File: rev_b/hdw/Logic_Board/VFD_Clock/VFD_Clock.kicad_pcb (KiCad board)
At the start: 4 copper layers, 200 x 50 mm, 359 parts, among them J1501 PICKIT4, J1801 I2C, J1802 USB UART, J201 +12V IN, J2401 USB_B_Mini, J3001 DSP_IO_Connector, Q1001 IRFL214TRPBF, Q1301 BSS214NW, Q1302 ZXMS6004FFTA, Q1304 BSS214NW, Q1306 ZXMS6004FFTA, Q1307 BSS214NW, Q1308 ZXMS6004FFTA, Q1501 BSS214NW, Q1801 BSS214NW, SW1501 MRST, U1001 TLV6700, U1002 LT3757, U1101 MCP9804, U1103 LTC4151DD, U1401 PIC32MZ2048EFG100_IPT, U1801 LTC6900, U1802 74LVC1G97, U1803 MCP9804, U1901 DS3231MZ, U1902 TLV6700, U2001 74LVC1G97, U2003 74LVC1G97, U2004 74LVC1G97, U2006 74LVC1G97, U201 TPS26600RHFT, U2101 TPS71533, U2102 74LVC1G97, U2103 74LVC1G97, U2104 74LVC1G97, U2105 74LVC1G97, U2106 74LVC1G97, U2107 74LVC1G97, U2108 74LVC1G97, U2201 TCA9803, U2301 DS1683, U2401 TLV6700, U2402 FT234XD, U2403 TPD3S014DBVR, U2404 SN74AVC2T245, U2601 INA219BxDCN, U2602 MCP9804, U2801 74VHC541, U2802 74VHC541, U2803 74LVC1G97, U2804 74LVC1G97, U2901 TCA9803, U2902 74VHC541, U301 INA219BxDCN, U302 MCP9804, U401 TPS62150A, U502 MCP9804, U503 INA219BxDCN, U601 TPS62150A, U702 MCP9804, U703 INA219BxDCN, U801 TPS62150A, U902 MCP9804, U903 INA219BxDCN, X1701 ASE-8.000MHz, X1702 ECS-327KE

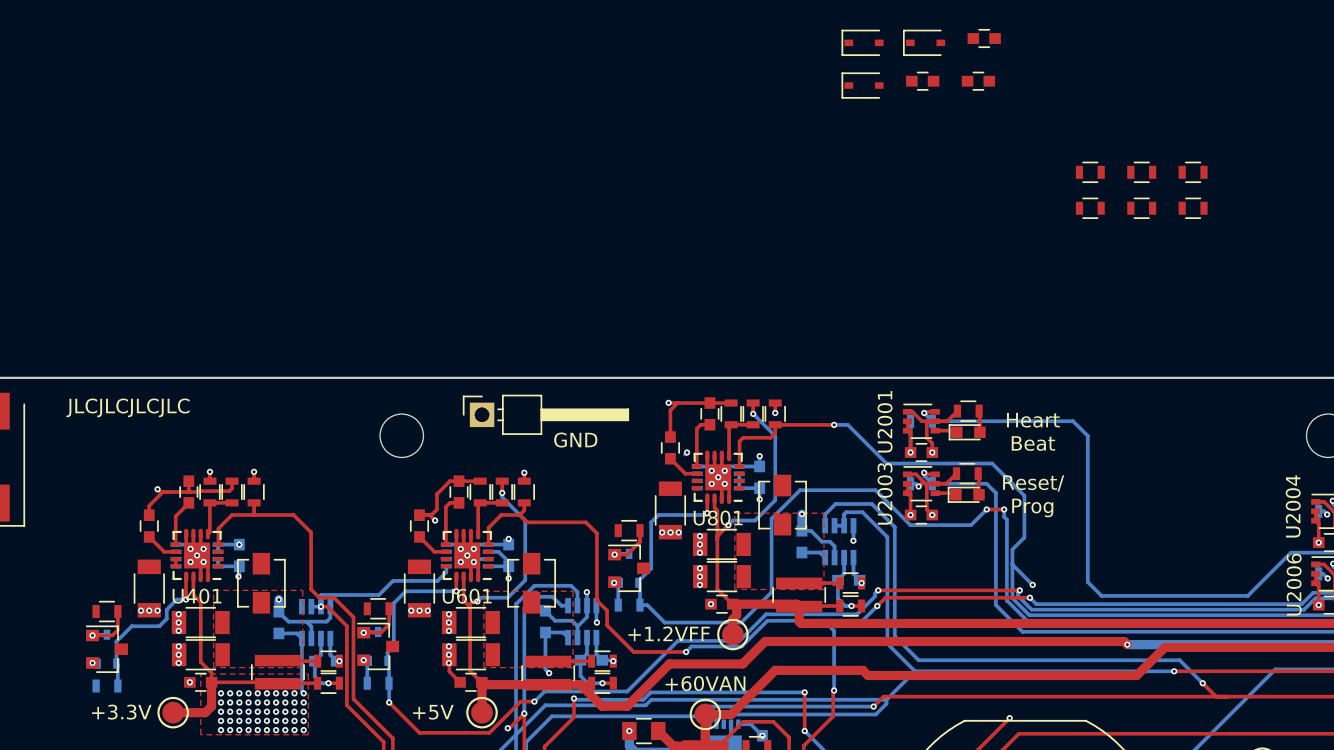
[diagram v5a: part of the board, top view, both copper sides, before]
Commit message: finished placing new parts
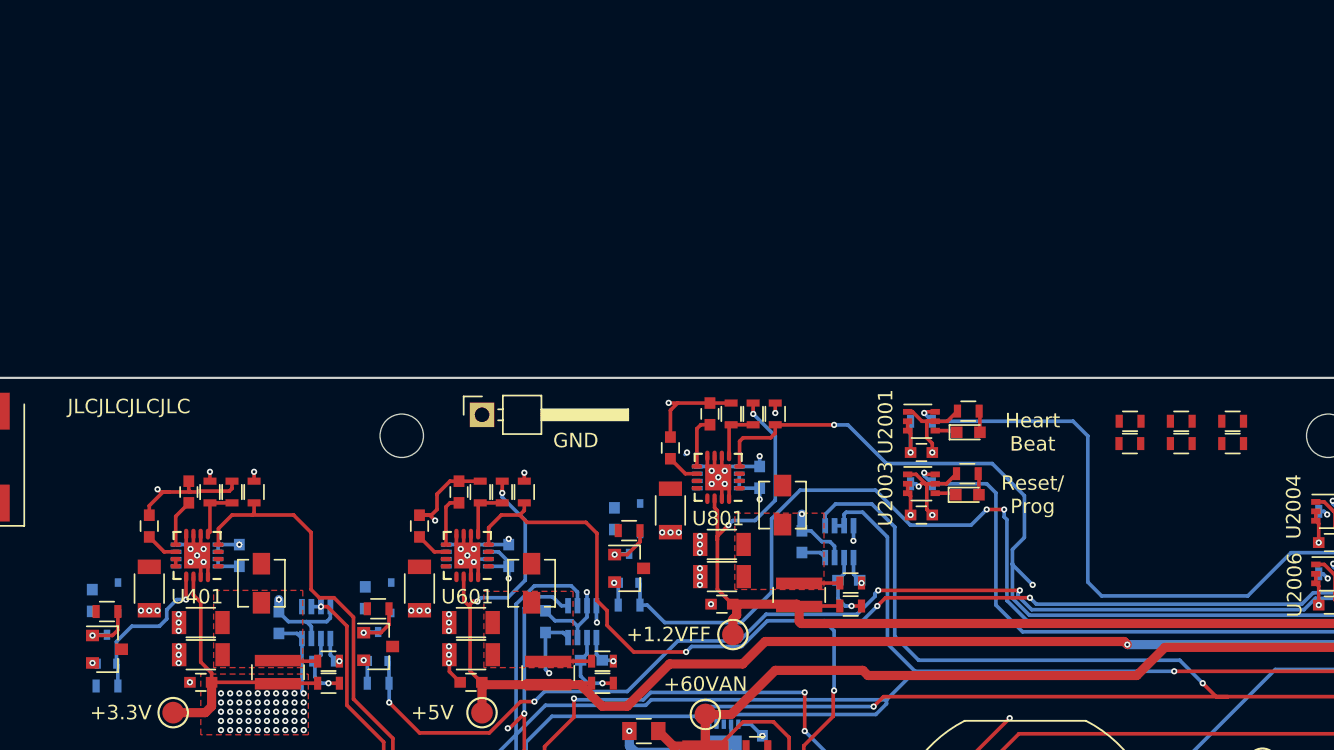
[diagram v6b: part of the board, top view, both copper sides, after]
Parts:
- C1301, C1302, C1303, D1301, D1302, D1303: moved to B.Cu
- moved C1301 67.7 mm to (81.0, 81.7), turned to 90 degrees
- moved D1301 64.2 mm to (82.7, 81.5), turned to 90 degrees
- moved C1302 57.6 mm to (99.8, 81.5), turned to 90 degrees
- moved D1302 48.2 mm to (101.6, 81.5), turned to 90 degrees
- moved C1303 39.3 mm to (117.0, 76.0), turned to 90 degrees
- moved D1303 38.3 mm to (118.8, 76.0), turned to 90 degrees
- moved R1802 17.4 mm to (152.7, 69.3)
- moved R1808 17.4 mm to (156.2, 69.3)
- moved R1810 17.4 mm to (159.7, 69.3)
- moved R1803 16.5 mm to (152.6, 70.8)
- moved R1809 16.5 mm to (156.2, 70.8)
- moved R1811 16.5 mm to (159.7, 70.8)
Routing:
- net I2C_SDA: track 257.9 -> 247.4 mm
- net POS5_RUN: track 119.2 -> 109.4 mm, vias 6 -> 5
- net POS1P2_VFF_RUN: track 105.6 -> 95.9 mm, vias 4 -> 3
- net +3V3: track 175.6 -> 174.8 mm, vias 88 -> 87

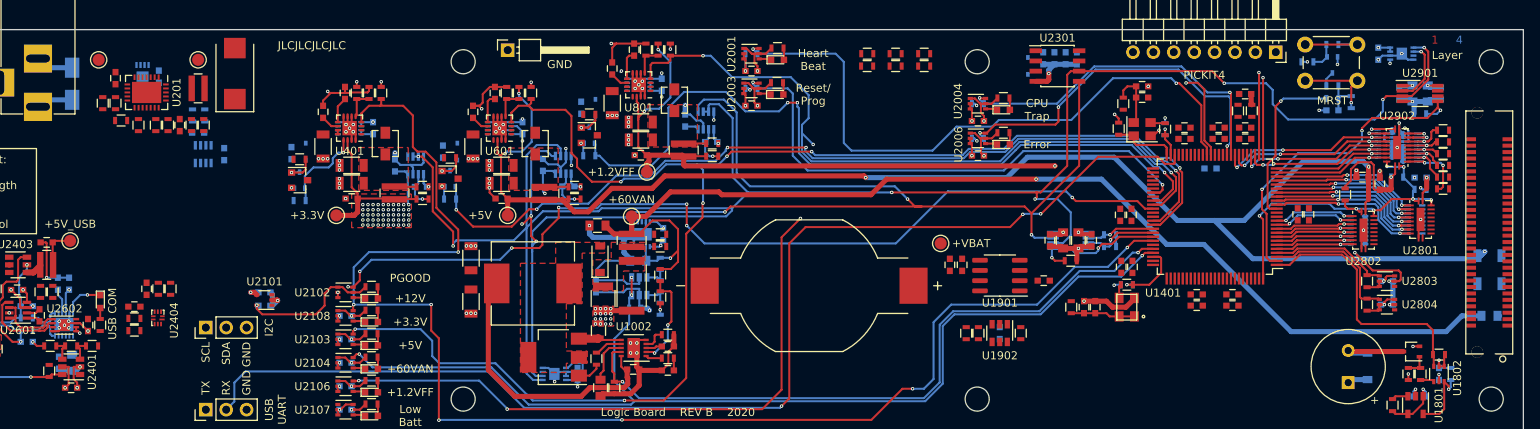
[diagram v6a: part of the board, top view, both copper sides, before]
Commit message: More rev B PCB routing
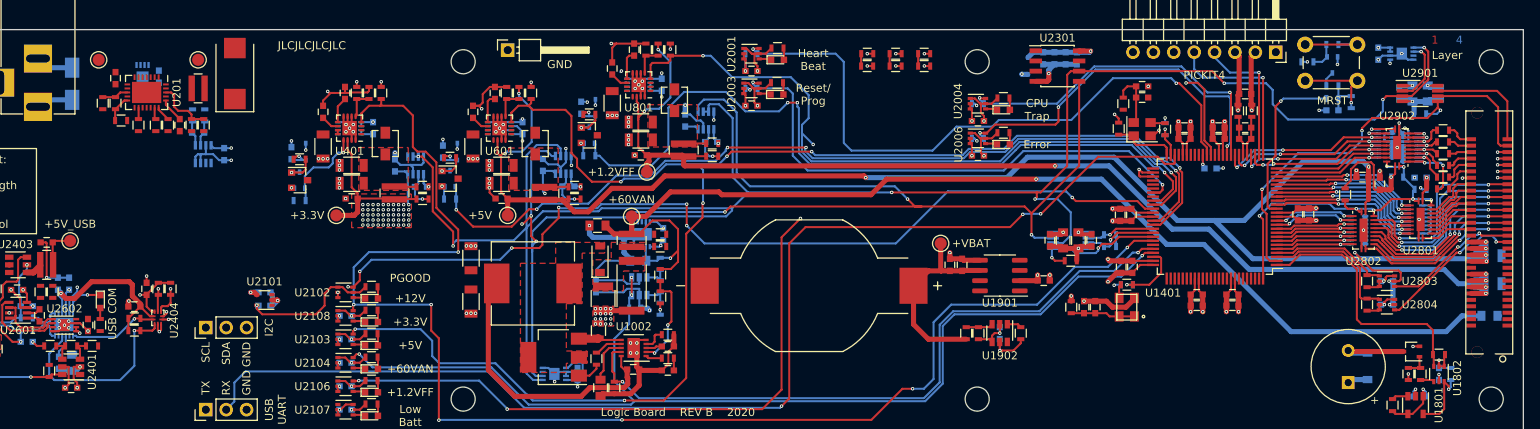
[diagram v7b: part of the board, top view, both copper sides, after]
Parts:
- turned R205 to 90 degrees
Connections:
- U1401 pad 70: Net-(U1401-Pad70) -> POS5_USB_PGOOD
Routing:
- net GND: track 280.5 -> 378.0 mm, vias 147 -> 178
- net +1.2VFF: track 77.5 -> 151.6 mm, vias 3 -> 7
- net +3V3: track 174.8 -> 240.1 mm, vias 87 -> 108
- net USB_UART_TX_BUF: track 0.00 -> 24.7 mm, vias 0 -> 1
- net VBAT: track 0.00 -> 24.6 mm
- net Grid_0_DSP: track 0.00 -> 24.3 mm, vias 0 -> 2
- net Grid_1_DSP: track 0.00 -> 23.6 mm, vias 0 -> 2
- net Grid_2_DSP: track 0.00 -> 22.8 mm, vias 0 -> 2
- net +3.3V_USB: track 3.15 -> 25.8 mm, vias 0 -> 1
- net Grid_3_DSP: track 0.00 -> 22.0 mm, vias 0 -> 2
- net Grid_4_DSP: track 0.00 -> 21.2 mm, vias 0 -> 2
- net Colon_1_DSP: track 0.00 -> 20.5 mm, vias 0 -> 2
- net Grid_5_DSP: track 0.00 -> 20.4 mm, vias 0 -> 2
- net Colon_0_DSP: track 0.00 -> 19.7 mm, vias 0 -> 2
- net Colon_3_DSP: track 0.00 -> 18.3 mm, vias 0 -> 2
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
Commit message: moar rev b rowting
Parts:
- turned R2406 to 90 degrees
- turned R2410 to 90 degrees
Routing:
- net GND: track 378.0 -> 409.4 mm, vias 178 -> 201
- net +5V_USB: track 8.24 -> 34.5 mm, vias 1 -> 4
- net VBAT_PGOOD: track 1.82 -> 27.2 mm
- net +12V: track 43.8 -> 57.5 mm, vias 1 -> 2
- net +60VAN: track 144.6 -> 158.0 mm, vias 2 -> 6
- net Net-(L2401-Pad2): track 0.00 -> 6.29 mm
- net +3V3: track 240.1 -> 246.3 mm, vias 108 -> 110
- net POS5_USB_SNS-: track 1.75 -> 6.47 mm
- net POS5_USB_SNS+: track 1.76 -> 5.41 mm
- net Net-(R205-Pad2): track 0.00 -> 2.66 mm, vias 0 -> 1
- net Net-(R2407-Pad2): track 2.16 -> 4.74 mm
- net POS12_PGOOD: track 121.3 -> 120.7 mm
- added copper zone on F.Cu, net +12V
- added copper zone on F.Cu, net +12Vin
- added copper zone on F.Cu, net Net-(L401-Pad1)
- added copper zone on F.Cu, net Net-(L601-Pad1)
- added copper zone on F.Cu, net Net-(L801-Pad1)
- added copper zone on F.Cu, net Net-(R205-Pad2)
